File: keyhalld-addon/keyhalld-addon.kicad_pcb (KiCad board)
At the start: 4 copper layers, 120 x 39.5 mm, 47 parts, among them J1 Conn_01x06_Pin, J2 USB_C_Receptacle_USB2.0_16P, J3 Conn_01x04_Pin, SW1 SW_Push, SW2 SW_Push, SW3 SW_Push, SW4 SW_Push, SW5 SW_Push, SW6 SW_Push, SW7 SW_Push, SW8 SW_Push, U1 TLV1117-33, U2 RP2350A, U3 USBLC6-2SC6, U4 ER_OLEDM0.91_1x-I2C, Y1 12MHz

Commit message: save the work
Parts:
- added S1: RKJXT1F42001, Library:XDCR_RKJXT1F42001, F.Cu at (143.0, 75.5)
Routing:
- net +3.3V: track 109.5 -> 0.00 mm, vias 12 -> 0
- net KEY1: track 89.8 -> 0.00 mm, vias 2 -> 0
- net KEY5: track 86.8 -> 0.00 mm, vias 2 -> 0
- net KEY2: track 71.6 -> 0.00 mm, vias 2 -> 0
- net KEY6: track 68.6 -> 0.00 mm, vias 2 -> 0
- net KEY3: track 53.1 -> 0.00 mm, vias 2 -> 0
- net KEY7: track 50.5 -> 0.00 mm, vias 2 -> 0
- net GND: track 49.8 -> 0.00 mm, vias 30 -> 0
- net +5V: track 44.5 -> 0.00 mm, vias 5 -> 0
- net MAG_UART_RX: track 35.9 -> 0.00 mm, vias 3 -> 0
- net MAG_UART_TX: track 33.6 -> 0.00 mm, vias 1 -> 0
- net KEY4: track 32.6 -> 0.00 mm, vias 2 -> 0
- net OLED_SDA: track 30.0 -> 0.00 mm, vias 1 -> 0
- net KEY8: track 28.3 -> 0.00 mm, vias 2 -> 0
- net OLED_SCL: track 28.2 -> 0.00 mm, vias 1 -> 0
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- removed copper zone on F.Cu, net +1V1
- removed copper zone on In1.Cu, net +1V1
- removed copper zone on F.Cu, net +3.3V
- removed copper zone on In1.Cu, net +3.3V
- removed copper zone on B.Cu, net GND
- removed copper zone on F.Cu, net GND

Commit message: maybe last schematic changes; pcb new layout
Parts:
- added D1: D, Diode_SMD:D_SOD-323, F.Cu at (187.5, 98.9)
- added D2: D, Diode_SMD:D_SOD-323, F.Cu at (187.5, 88.5)
- added H1: MountingHole_Pad, MountingHole:MountingHole_2.2mm_M2_DIN965_Pad, F.Cu at (70.0, 82.5)
- added H2: MountingHole_Pad, MountingHole:MountingHole_2.2mm_M2_DIN965_Pad, F.Cu at (128.5, 82.5)
- added H3: MountingHole_Pad, MountingHole:MountingHole_2.2mm_M2_DIN965_Pad, F.Cu at (70.0, 117.5)
- added H4: MountingHole_Pad, MountingHole:MountingHole_2.2mm_M2_DIN965_Pad, F.Cu at (128.5, 117.5)
- added R15: 10K, Resistor_SMD:R_0603_1608Metric_Pad0.98x0.95mm_HandSolder, F.Cu at (68.5, 104.0)
- added R16: 10K, Resistor_SMD:R_0603_1608Metric_Pad0.98x0.95mm_HandSolder, F.Cu at (88.0, 104.1)
- added R17: 10K, Resistor_SMD:R_0603_1608Metric_Pad0.98x0.95mm_HandSolder, F.Cu at (107.5, 104.0)
- added R18: 10K, Resistor_SMD:R_0603_1608Metric_Pad0.98x0.95mm_HandSolder, F.Cu at (127.0, 104.0)
- added R19: 1K, Resistor_SMD:R_0603_1608Metric_Pad0.98x0.95mm_HandSolder, F.Cu at (159.0, 115.5)
- added R20: 4K7, Resistor_SMD:R_0603_1608Metric_Pad0.98x0.95mm_HandSolder, F.Cu at (155.5, 85.0)
- added R21: 4K7, Resistor_SMD:R_0603_1608Metric_Pad0.98x0.95mm_HandSolder, F.Cu at (155.5, 87.0)
- added R22: 5K1, Resistor_SMD:R_0603_1608Metric_Pad0.98x0.95mm_HandSolder, F.Cu at (172.5, 84.0)
- added R23: 5K1, Resistor_SMD:R_0603_1608Metric_Pad0.98x0.95mm_HandSolder, F.Cu at (172.5, 85.5)
- added R24: 1.5K, Resistor_SMD:R_0603_1608Metric_Pad0.98x0.95mm_HandSolder, F.Cu at (176.5, 90.5)
- added SW10: RST, Button_Switch_SMD:SW_Tactile_SPST_NO_Straight_CK_PTS636Sx25SMTRLFS, F.Cu at (177.5, 116.0)
- added SW9: BOOT, Button_Switch_SMD:SW_Tactile_SPST_NO_Straight_CK_PTS636Sx25SMTRLFS, F.Cu at (167.5, 116.0)
- R11: value 1K -> 10K
- R12, R13: value 5K1 -> 22R
- R14: value 1.5K -> 4K7
- R5, R6: value 22R -> 10K
- moved R8 64.6 mm to (68.5, 96.0), turned to 90 degrees
- moved R9 47.6 mm to (88.0, 96.0), turned to 90 degrees
- moved U3 39.5 mm to (180.0, 90.5)
- moved J2 39.5 mm to (180.0, 83.5)
- moved R11 31.5 mm to (127.0, 95.9), turned to 90 degrees
- moved R10 31.0 mm to (107.5, 95.9), turned to 90 degrees
- moved C9 28.5 mm to (172.5, 104.0), turned to 0 degrees
- moved C12 28.4 mm to (185.5, 100.0)
- moved U1 25.3 mm to (180.0, 99.0), turned to 180 degrees
- moved C11 25.3 mm to (185.5, 96.5), turned to 90 degrees
- moved S1 24.7 mm to (140.0, 100.0)
- moved J3 23.1 mm to (187.5, 102.4), turned to -90 degrees
- moved J1 22.6 mm to (146.3, 115.6), turned to -90 degrees
- moved R13 21.0 mm to (166.0, 96.5), turned to -90 degrees
- moved U4 20.1 mm to (152.0, 92.3)
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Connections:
- J2 pad A4: +5V -> Net-(D2-A)
- J2 pad A9: +5V -> Net-(D2-A)
- J2 pad B4: +5V -> Net-(D2-A)
- J2 pad B9: +5V -> Net-(D2-A)
- J3 pad 1: +5V -> Net-(D1-K)
- R1 pad 2: KEY1 -> EN_S_A
- R10 pad 2: KEY8 -> KEY3
- R11 pad 1: XOUT -> +3.3V
- R11 pad 2: Net-(C16-Pad2) -> KEY4
- R12 pad 1: Net-(J2-CC1) -> Net-(U2-USB_DP)
- R12 pad 2: GND -> D+
- R13 pad 1: GND -> D-
- R13 pad 2: Net-(J2-CC2) -> Net-(U2-USB_DM)
- R14 pad 1: /CONN_D+ -> Net-(U2-QSPI_~{SS})
- R14 pad 2: +3.3V -> BOOT
- R2 pad 1: +3.3V -> EN_S_B
- R2 pad 2: KEY2 -> +3.3V
- R3 pad 2: KEY3 -> EN_A
- R4 pad 1: +3.3V -> EN_B
- R4 pad 2: KEY4 -> +3.3V
- R5 pad 1: Net-(U2-USB_DP) -> +3.3V
- R5 pad 2: D+ -> EN_S_P
- R6 pad 1: D- -> EN_S_C
- R6 pad 2: Net-(U2-USB_DM) -> +3.3V
- R7 pad 2: KEY5 -> EN_S_D
- R8 pad 2: KEY6 -> KEY1
- R9 pad 2: KEY7 -> KEY2
- S1 pad A: unconnected-(S1-PadA) -> EN_S_A
- S1 pad B: unconnected-(S1-PadB) -> EN_S_B
- S1 pad C: unconnected-(S1-PadC) -> EN_S_C
- S1 pad COM: unconnected-(S1-PadCOM) -> GND
- S1 pad D: unconnected-(S1-PadD) -> EN_S_D
- S1 pad EN_A: unconnected-(S1-PadEN_A) -> EN_A
- S1 pad EN_B: unconnected-(S1-PadEN_B) -> EN_B
- S1 pad EN_COM: unconnected-(S1-PadEN_COM) -> GND
- S1 pad GND: unconnected-(S1-PadGND) -> GND
- S1 pad P: unconnected-(S1A-PUSH-PadP) -> EN_S_P
- U2 pad 31: unconnected-(U2-GPIO19-Pad31) -> EN_A
- U2 pad 32: unconnected-(U2-GPIO20-Pad32) -> EN_B
- U2 pad 33: unconnected-(U2-GPIO21-Pad33) -> EN_S_P
- U2 pad 34: unconnected-(U2-GPIO22-Pad34) -> EN_S_A
- U2 pad 35: unconnected-(U2-GPIO23-Pad35) -> EN_S_B
- U2 pad 36: unconnected-(U2-GPIO24-Pad36) -> EN_S_C
- U2 pad 37: unconnected-(U2-GPIO25-Pad37) -> EN_S_D
- U2 pad 59: unconnected-(U2-QSPI_SD1-Pad59) -> GND
- U2 pad 60: unconnected-(U2-QSPI_~{SS}-Pad60) -> Net-(U2-QSPI_~{SS})
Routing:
- added copper zone on B.Cu, net GND
- added copper zone on F.Cu, net GND
- added copper zone on In1.Cu, net GND
- added copper zone on In2.Cu, net GND
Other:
- board size 120 x 39.5 mm -> 140 x 40 mm
- board text added: "5V"
- board text added: "GND"
- board text added: "RX"
- board text added: "TX"

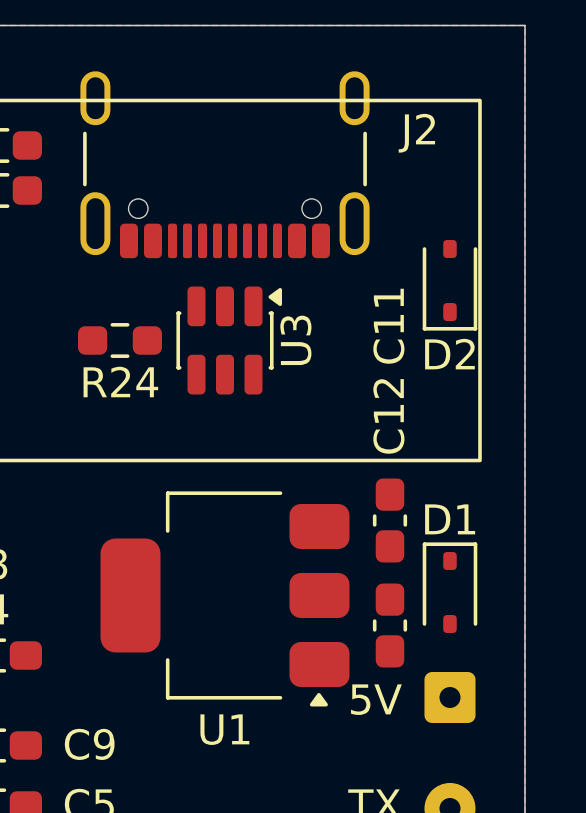
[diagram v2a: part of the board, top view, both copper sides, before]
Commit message: fix diodes
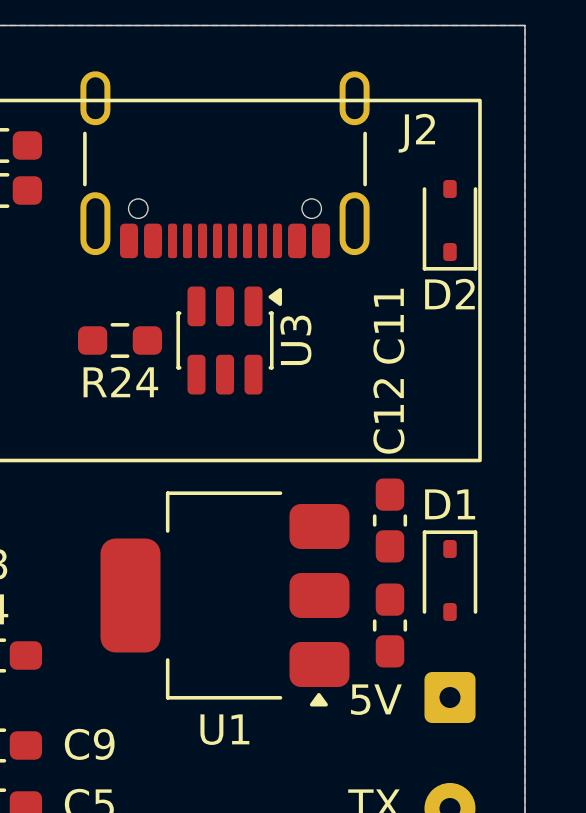
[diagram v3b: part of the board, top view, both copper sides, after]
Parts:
- moved D2 2.00 mm to (187.5, 86.5)
- moved D1 0.40 mm to (187.5, 98.5)
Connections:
- D1 pad 1: Net-(D1-K) -> +5V
- D1 pad 2: +5V -> Net-(D1-A)
- J3 pad 1: Net-(D1-K) -> Net-(D1-A)

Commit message: Super changes; FInal!
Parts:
- added D10: WS2812B-2020, LED_SMD:LED_WS2812B-2020_PLCC4_2.0x2.0mm, F.Cu at (131.8, 67.8)
- added D11: WS2812B-2020, LED_SMD:LED_WS2812B-2020_PLCC4_2.0x2.0mm, F.Cu at (131.8, 71.4)
- added D3: WS2812B-2020 STATUS, LED_SMD:LED_WS2812B-2020_PLCC4_2.0x2.0mm, F.Cu at (123.2, 64.3)
- added D4: WS2812B-2020, LED_SMD:LED_WS2812B-2020_PLCC4_2.0x2.0mm, F.Cu at (123.2, 67.8)
- added D5: WS2812B-2020, LED_SMD:LED_WS2812B-2020_PLCC4_2.0x2.0mm, F.Cu at (123.2, 71.4)
- added D6: WS2812B-2020, LED_SMD:LED_WS2812B-2020_PLCC4_2.0x2.0mm, F.Cu at (127.5, 64.3)
- added D7: WS2812B-2020, LED_SMD:LED_WS2812B-2020_PLCC4_2.0x2.0mm, F.Cu at (127.5, 67.8)
- added D8: WS2812B-2020, LED_SMD:LED_WS2812B-2020_PLCC4_2.0x2.0mm, F.Cu at (127.5, 71.4)
- added D9: WS2812B-2020, LED_SMD:LED_WS2812B-2020_PLCC4_2.0x2.0mm, F.Cu at (131.8, 64.3)
- J3: footprint Connector_Wire:SolderWire-0.127sqmm_1x04_P3.7mm_D0.48mm_OD1mm -> Connector_PinHeader_2.54mm:PinHeader_1x04_P2.54mm_Vertical
- moved J3 4.29 mm to (187.5, 106.7), turned to 0 degrees
- renumbered D2 to D1, D1 to D2
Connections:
- U2 pad 41: unconnected-(U2-GPIO27_ADC1-Pad41) -> WS_LED

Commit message: routed pcb for addon board
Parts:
- added C17: 100n, Capacitor_SMD:C_0603_1608Metric, F.Cu at (140.0, 82.0)
- added C18: 100n, Capacitor_SMD:C_0603_1608Metric, F.Cu at (60.0, 82.0)
- added C19: 100n, Capacitor_SMD:C_0603_1608Metric, F.Cu at (79.5, 82.0)
- added C20: 100n, Capacitor_SMD:C_0603_1608Metric, F.Cu at (99.0, 82.0)
- added C21: 100n, Capacitor_SMD:C_0603_1608Metric, F.Cu at (118.5, 82.0)
- added C22: 100n, Capacitor_SMD:C_0603_1608Metric, F.Cu at (60.0, 102.0)
- added C23: 100n, Capacitor_SMD:C_0603_1608Metric, F.Cu at (79.5, 102.0)
- added C24: 100n, Capacitor_SMD:C_0603_1608Metric, F.Cu at (99.0, 102.0)
- added C25: 100n, Capacitor_SMD:C_0603_1608Metric, F.Cu at (118.5, 102.0)
- D3: value WS2812B-2020 STATUS -> STATUS
- moved D8 75.2 mm to (60.0, 104.5)
- moved D9 66.0 mm to (79.5, 104.5)
- moved D4 65.3 mm to (60.0, 84.5)
- moved D10 49.2 mm to (99.0, 104.5)
- moved D5 45.6 mm to (79.5, 84.5)
- moved D11 35.7 mm to (118.5, 104.5)
- moved D6 34.9 mm to (99.0, 84.5)
- moved D3 26.3 mm to (140.0, 84.5)
- moved D7 18.9 mm to (118.5, 84.5)
- moved J3 1.25 mm to (186.2, 106.7)
- moved SW1 0.08 mm to (60.0, 90.0)
- moved SW2 0.08 mm to (79.5, 90.0)
- moved SW3 0.08 mm to (99.0, 90.0)
- moved SW4 0.08 mm to (118.5, 90.0)
- moved SW5 0.08 mm to (60.0, 110.0)
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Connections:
- net Net-(U2-USB_DM) renamed /USB_D-
- net Net-(U2-USB_DP) renamed /USB_D+
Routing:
- net +5V: track 0.00 -> 260.7 mm, vias 0 -> 11
- net +3.3V: track 0.00 -> 243.6 mm, vias 0 -> 17
- net KEY1: track 0.00 -> 109.3 mm, vias 0 -> 3
- net KEY5: track 0.00 -> 107.6 mm, vias 0 -> 2
- net KEY2: track 0.00 -> 89.6 mm, vias 0 -> 2
- net KEY6: track 0.00 -> 88.2 mm, vias 0 -> 2
- net Net-(D3-DOUT): track 0.00 -> 80.7 mm
- net Net-(D7-DOUT): track 0.00 -> 75.9 mm, vias 0 -> 2
- net GND: track 0.00 -> 74.2 mm, vias 0 -> 53
- net KEY3: track 0.00 -> 70.1 mm, vias 0 -> 2
- net KEY7: track 0.00 -> 69.3 mm, vias 0 -> 2
- net KEY8: track 0.00 -> 49.1 mm, vias 0 -> 2
- net EN_A: track 0.00 -> 48.8 mm, vias 0 -> 1
- net KEY4: track 0.00 -> 47.9 mm, vias 0 -> 4
- net EN_S_D: track 0.00 -> 47.1 mm, vias 0 -> 3
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- added copper zone on F.Cu, net +1V1
- added copper zone on F.Cu, net +3.3V
- added copper zone on In1.Cu, net +3.3V
- added copper zone on F.Cu, net +5V

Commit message: stitching vias; one more hole
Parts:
- added H5: MountingHole_Pad, MountingHole:MountingHole_2.2mm_M2_DIN965_Pad, F.Cu at (180.0, 108.0)
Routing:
- net GND: vias 53 -> 282

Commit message: fix for dvdd
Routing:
- net GND: track 74.2 -> 76.5 mm
- net +3.3V: track 243.6 -> 244.3 mm, vias 17 -> 15
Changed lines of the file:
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@@
 			(net "GND")
 			(pintype "passive")
+			(zone_connect 2)
 		)
 		(embedded_fonts no)
@@
 		(tags "SOT TO_SOT_SMD")
 		(property "Reference" "U3"
-			(at 0 -2.4 90)
+			(at 0 -2.5 180)
 			(layer "F.SilkS")
 			(effects
@@
 			(net "GND")
 			(pintype "passive")
+			(zone_connect 2)
 		)
 		(embedded_fonts no)
@@
 	)
 	(segment
-		(start 167.8 101.55)
-		(end 167.8 100.7)
-		(width 0.2)
-		(layer "F.Cu")
-		(net "+3.3V")
-	)
-	(segment
 		(start 164.6 101.55)
 		(end 164.6 100.6)
@@
 	)
 	(segment
+		(start 167.348529 99.5)
+		(end 167.725 99.5)
+		(width 0.2)
+		(layer "F.Cu")
+		(net "+3.3V")
+	)
+	(segment
 		(start 168.45 105)
 		(end 167.5 105)
@@
 	)
 	(segment
-		(start 169 100.5)
-		(end 170 100.5)
-		(width 0.2)
-		(layer "F.Cu")
-		(net "+3.3V")
-	)
-	(segment
 		(start 136.5875 110.5)
 		(end 136.5875 111.0875)
@@
 	)
 	(segment
-		(start 167.725 100.225)
-		(end 168 100.5)
-		(width 0.2)
-		(layer "F.Cu")
-		(net "+3.3V")
-	)
-	(segment
 		(start 168.1375 111.5)
 		(end 168.1375 110.6375)
@@
 	)
 	(segment
-		(start 127 96.825)
-		(end 127 98)
+		(start 166.6 101.55)
+		(end 166.6 100.248529)
 		(width 0.2)
 		(layer "F.Cu")
@@
 	)
 	(segment
-		(start 168.1375 110.6375)
-		(end 168 110.5)
+		(start 127 96.825)
+		(end 127 98)
 		(width 0.2)
 		(layer "F.Cu")
@@
 	)
 	(segment
-		(start 167.8 100.7)
-		(end 168 100.5)
+		(start 168.1375 110.6375)
+		(end 168 110.5)
 		(width 0.2)
 		(layer "F.Cu")
@@
 	)
 	(segment
-		(start 163.8 108.45)
-		(end 163.8 108.885789)
+		(start 167.725 99.5)
+		(end 167.775 99.5)
 		(width 0.2)
 		(layer "F.Cu")
@@
 	)
 	(segment
-		(start 156.4125 87)
-		(end 157.5 87)
+		(start 163.8 108.45)
+		(end 163.8 108.885789)
 		(width 0.2)
 		(layer "F.Cu")
@@
 	)
 	(segment
-		(start 170 100.5)
-		(end 170.5 101)
+		(start 156.4125 87)
+		(end 157.5 87)
 		(width 0.2)
 		(layer "F.Cu")
@@
 	)
 	(segment
+		(start 166.6 100.248529)
+		(end 167.348529 99.5)
+		(width 0.2)
+		(layer "F.Cu")
+		(net "+3.3V")
+	)
+	(segment
 		(start 142.9125 110.5)
 		(end 143.45625 111.04375)
@@
 	)
 	(segment
+		(start 168.7 101)
+		(end 170.5 101)
+		(width 0.2)
+		(layer "F.Cu")
+		(net "+3.3V")
+	)
+	(segment
 		(start 158.3625 101)
 		(end 159.5 101)
@@
 	)
 	(segment
+		(start 167.8 101.55)
+		(end 168.15 101.55)
+		(width 0.2)
+		(layer "F.Cu")
+		(net "+3.3V")
+	)
+	(segment
 		(start 129.5 100.4125)
 		(end 130.5875 100.4125)
@@
 	)
 	(segment
-		(start 168 100.5)
-		(end 169 100.5)
-		(width 0.2)
-		(layer "F.Cu")
-		(net "+3.3V")
-	)
-	(segment
 		(start 88 102)
 		(end 88 98)
@@
 	)
 	(segment
-		(start 167.725 99.5)
-		(end 167.725 100.225)
+		(start 168.15 101.55)
+		(end 168.7 101)
 		(width 0.2)
 		(layer "F.Cu")
@@
 	)
 	(via
-		(at 168 100.5)
-		(size 0.6)
-		(drill 0.3)
-		(layers "F.Cu" "B.Cu")
-		(net "+3.3V")
-	)
-	(via
 		(at 157.5 85)
 		(size 0.6)
@@
 	)
 	(via
-		(at 169 100.5)
-		(size 0.6)
-		(drill 0.3)
-		(layers "F.Cu" "B.Cu")
-		(net "+3.3V")
-	)
-	(via
 		(at 162.5 98.5)
 		(size 0.6)
@@
 	)
 	(segment
-		(start 169.275 99.5)
-		(end 170 99.5)
+		(start 155.825 112.675)
+		(end 156 112.5)
 		(width 0.2)
 		(layer "F.Cu")
@@
 	)
 	(segment
-		(start 155.825 112.675)
-		(end 156 112.5)
+		(start 165 112.8625)
+		(end 165 114)
 		(width 0.2)
 		(layer "F.Cu")
@@
 	)
 	(segment
-		(start 165 112.8625)
-		(end 165 114)
+		(start 167.4 101.1)
+		(end 167.9 100.6)
 		(width 0.2)
 		(layer "F.Cu")
@@
 	)
 	(segment
+		(start 167.4 101.55)
+		(end 167.4 101.1)
+		(width 0.2)
+		(layer "F.Cu")
+		(net "GND")
+	)
+	(segment
 		(start 139.085 85.05)
 		(end 139.085 85.915)
@@
 	)
 	(segment
+		(start 169.275 99.5)
+		(end 168.175 100.6)
+		(width 0.2)
+		(layer "F.Cu")
+		(net "GND")
+	)
+	(segment
 		(start 180 89.3625)
 		(end 180 90.5)
@@
 	)
 	(segment
+		(start 168.175 100.6)
+		(end 167.9 100.6)
+		(width 0.2)
+		(layer "F.Cu")
+		(net "GND")
+	)
+	(segment
 		(start 156.6375 104)
 		(end 155.5 104)
@@
 	)
 	(via
+		(at 170 99.5)
+		(size 0.5)
+		(drill 0.3)
+		(layers "F.Cu" "B.Cu")
+		(net "GND")
+	)
+	(via
 		(at 74.8505 98.8505)
 		(size 0.6)
@@
 	)
 	(via
-		(at 170 99.5)
-		(size 0.5)
-		(drill 0.3)
-		(layers "F.Cu" "B.Cu")
-		(net "GND")
-	)
-	(via
 		(at 185.8505 89.8505)
 		(size 0.6)
@@
 	)
 	(segment
-		(start 167.201704 100.552229)
-		(end 167.201704 100.640397)
+		(start 167.182086 100.559372)
+		(end 167.231744 100.60903)
 		(width 0.2)
 		(layer "F.Cu")
@@
 	)
 	(segment
+		(start 167.231744 100.610357)
+		(end 167 100.842101)
+		(width 0.2)
+		(layer "F.Cu")
+		(net "Net-(U2-VREG_LX)")
+	)
+	(segment
+		(start 167.231744 100.60903)
+		(end 167.231744 100.610357)
+		(width 0.2)
+		(layer "F.Cu")
+		(net "Net-(U2-VREG_LX)")
+	)
+	(segment
 		(start 169.225 96.896001)
 		(end 169.353999 97.025)
@@
 	)
 	(segment
-		(start 167.201704 100.640397)
-		(end 167 100.842101)
+		(start 167.182086 100.540096)
+		(end 167.182086 100.559372)
 		(width 0.2)
 		(layer "F.Cu")
@@
 	)
 	(via
-		(at 167.201704 100.552229)
-		(size 0.6)
+		(at 167.182086 100.540096)
+		(size 0.5)
 		(drill 0.3)
 		(layers "F.Cu" "B.Cu")
@@
 	)
 	(segment
-		(start 167.6 98.8)
-		(end 168.2 98.8)
+		(start 169.075 97.025)
+		(end 169.353999 97.025)
 		(width 0.2)
 		(layer "B.Cu")
@@
 	)
 	(segment
-		(start 169.075 97.025)
-		(end 169.353999 97.025)
+		(start 168.5 98.5)
+		(end 168.5 97.6)
 		(width 0.2)
 		(layer "B.Cu")
@@
 	)
 	(segment
-		(start 167.201704 100.552229)
-		(end 167.201704 99.198296)
+		(start 167.201704 99.198296)
+		(end 167.6 98.8)
 		(width 0.2)
 		(layer "B.Cu")
@@
 	)
 	(segment
-		(start 168.5 98.5)
-		(end 168.5 97.6)
+		(start 167.182086 100.540096)
+		(end 167.172448 100.530458)
+		(width 0.2)
+		(layer "B.Cu")
+		(net "Net-(U2-VREG_LX)")
+	)
+	(segment
+		(start 167.172448 100.390412)
+		(end 167.2 100.36286)
+		(width 0.2)
+		(layer "B.Cu")
+		(net "Net-(U2-VREG_LX)")
+	)
+	(segment
+		(start 168.5 97.6)
+		(end 169.075 97.025)
+		(width 0.2)
+		(layer "B.Cu")
+		(net "Net-(U2-VREG_LX)")
+	)
+	(segment
+		(start 167.6 98.8)
+		(end 168.2 98.8)
+		(width 0.2)
+		(layer "B.Cu")
+		(net "Net-(U2-VREG_LX)")
+	)
+	(segment
+		(start 167.2 100.337675)
+		(end 167.201704 100.335971)
 		(width 0.2)
 		(layer "B.Cu")
@@
 	)
 	(segment
-		(start 167.201704 99.198296)
-		(end 167.6 98.8)
+		(start 167.172448 100.530458)
+		(end 167.172448 100.390412)
 		(width 0.2)
 		(layer "B.Cu")
@@
 	)
 	(segment
-		(start 168.5 97.6)
-		(end 169.075 97.025)
+		(start 167.2 100.36286)
+		(end 167.2 100.337675)
+		(width 0.2)
+		(layer "B.Cu")
+		(net "Net-(U2-VREG_LX)")
+	)
+	(segment
+		(start 167.201704 100.335971)
+		(end 167.201704 99.198296)
 		(width 0.2)
 		(layer "B.Cu")
@@
 	)
 	(zone
-		(net "+3.3V")
-		(layer "F.Cu")
-		(hatch edge 0.5)
-		(priority 4)
-		(connect_pads
-			(clearance 0.2)
-		)
-		(min_thickness 0.2)
-		(fill yes
-			(thermal_gap 0.5)
-			(thermal_bridge_width 0.5)
-			(island_removal_mode 0)
-		)
-		(polygon
-			(pts
-				(xy 168.2 99) (xy 167.3 99) (xy 167.3 100) (xy 168 100.8) (xy 169 100.8) (xy 169 100.2) (xy 168.5 100.2)
-			)
-		)
-	)
-	(zone
 		(net "+5V")
 		(layer "F.Cu")
@@
 			(pts
 				(xy 166.1 100.2) (xy 166.1 98.2) (xy 167 97.9) (xy 167.5 96.7) (xy 168.1 96.7) (xy 168.2 97.7) (xy 168.2 98.5)
-				(xy 167.3 98.5) (xy 167 98.7) (xy 167 99.8) (xy 166.3 100.8)
+				(xy 167.3 98.5) (xy 167 98.7) (xy 166.3 100.1) (xy 166.3 100.8)
 			)
 		)

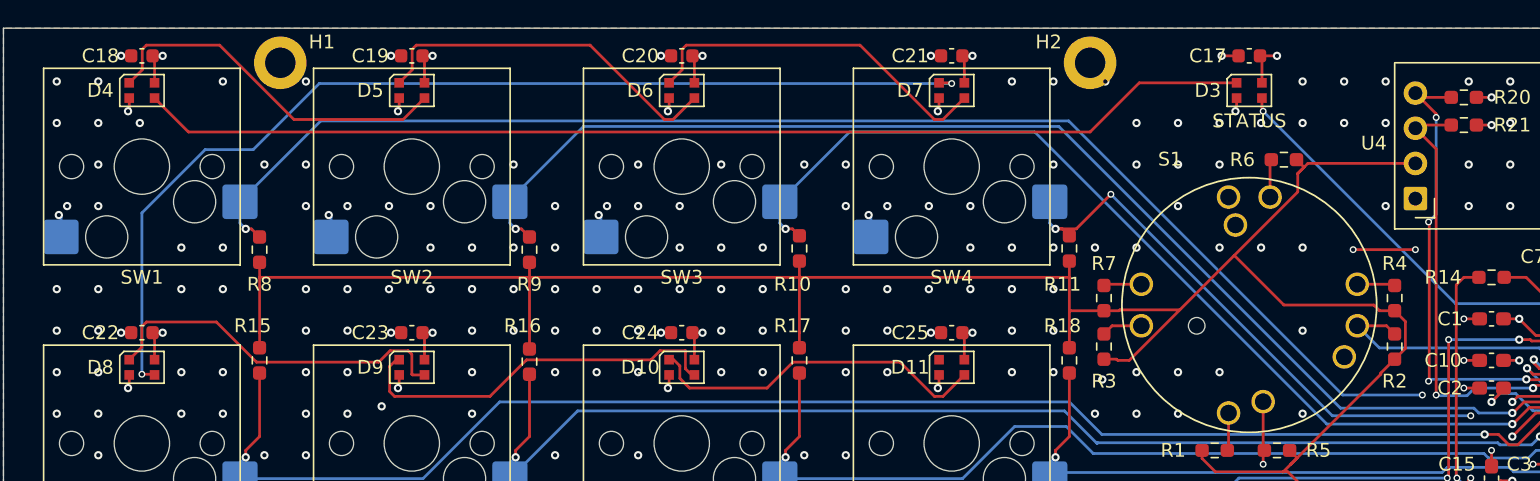
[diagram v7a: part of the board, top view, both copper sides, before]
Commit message: move ws leds .4mm down to fin under huano sakura switch
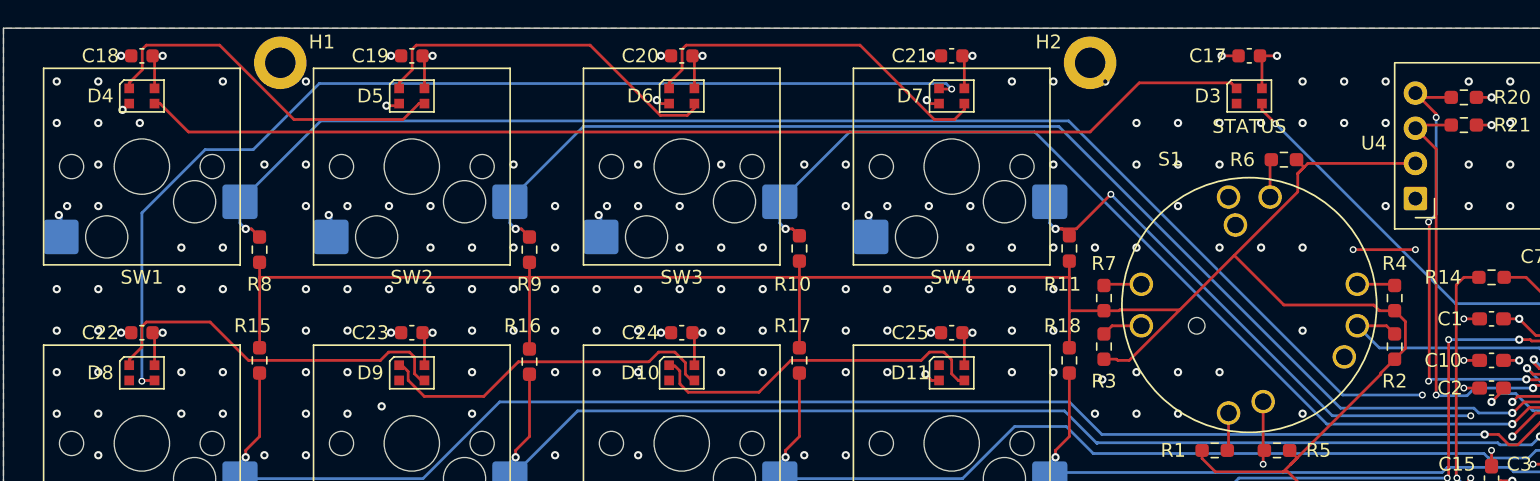
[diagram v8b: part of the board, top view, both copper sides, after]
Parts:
- moved D10 0.40 mm to (99.0, 104.9)
- moved D11 0.40 mm to (118.5, 104.9)
- moved D3 0.40 mm to (140.0, 84.9)
- moved D4 0.40 mm to (60.0, 84.9)
- moved D5 0.40 mm to (79.5, 84.9)
- moved D6 0.40 mm to (99.0, 84.9)
- moved D7 0.40 mm to (118.5, 84.9)
- moved D8 0.40 mm to (60.0, 104.9)
- moved D9 0.40 mm to (79.5, 104.9)
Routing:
- net GND: track 76.5 -> 72.4 mm, vias 282 -> 278
- net +5V: track 260.7 -> 264.3 mm
- net Net-(D10-DIN): track 27.7 -> 25.3 mm
- net Net-(D7-DOUT): track 75.9 -> 76.6 mm
